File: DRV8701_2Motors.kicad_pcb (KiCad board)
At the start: 4 copper layers, 100 x 40 mm, 92 parts, among them J1 Conn_01x02, J10 Conn_01x04, J11 Conn_01x03, J2 Conn_01x10, J3 Conn_01x10, J4 Conn_01x02, J5 Conn_01x02, J6 Conn_01x04, J7 Conn_ST_STDC14, J8 Conn_01x03, J9 Conn_01x04, SW1 SW_SPDT_321, U16 STM32F303RETx, U3 AM26LV32xD, U4 AM26LV32xD

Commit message: maj README img
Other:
- board text added: "Battery Level"
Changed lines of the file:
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@@
 			(effects
 				(font
-					(size 1 1)
-					(thickness 0.15)
+					(size 0.8 0.5)
+					(thickness 0.1)
+					(bold yes)
 				)
 			)
@@
 			(effects
 				(font
-					(size 1 1)
+					(size 0.8 0.5)
 					(thickness 0.1)
+					(bold yes)
 				)
 			)
@@
 			(effects
 				(font
-					(size 1 1)
+					(size 0.8 0.5)
 					(thickness 0.1)
 				)
@@
 			(effects
 				(font
-					(size 1 1)
+					(size 0.8 0.5)
 					(thickness 0.1)
+					(bold yes)
 				)
 			)
@@
 		(tags "Surface mounted pin header SMD 2x05 1.27mm double row")
 		(property "Reference" "J3"
-			(at 4.8 -1.95 0)
+			(at 4.21 -1.87 0)
 			(layer "F.SilkS")
 			(effects
@@
 		(tags "connector JST PH vertical")
 		(property "Reference" "J11"
-			(at 5.79 -3.31 0)
+			(at 5.9 -2.81 0)
 			(layer "F.SilkS")
 			(effects
 				(font
-					(size 1 1)
-					(thickness 0.15)
+					(size 0.8 0.5)
+					(thickness 0.1)
+					(bold yes)
 				)
 			)
@@
 		(tags "LED RGB NeoPixel PLCC-4 5050")
 		(property "Reference" "D2"
-			(at -0.12 1.79 0)
+			(at -4.17 1.84 0)
 			(layer "F.SilkS")
 			(effects
 				(font
-					(size 1 1)
-					(thickness 0.15)
+					(size 0.8 0.5)
+					(thickness 0.1)
+					(bold yes)
 				)
 			)
@@
 			(effects
 				(font
-					(size 1 1)
-					(thickness 0.15)
+					(size 0.8 0.5)
+					(thickness 0.1)
+					(bold yes)
 				)
 			)
@@
 			(effects
 				(font
-					(size 1 1)
-					(thickness 0.15)
+					(size 0.8 0.5)
+					(thickness 0.1)
+					(bold yes)
 				)
 			)
@@
 			(effects
 				(font
-					(size 1 1)
+					(size 0.8 0.5)
 					(thickness 0.1)
 				)
@@
 			(effects
 				(font
-					(size 1 1)
+					(size 0.8 0.5)
 					(thickness 0.1)
 				)
@@
 			(effects
 				(font
-					(size 0.8 0.8)
+					(size 0.8 0.5)
 					(thickness 0.1)
 					(bold yes)
@@
 			(effects
 				(font
-					(size 1 1)
+					(size 0.8 0.5)
 					(thickness 0.1)
 				)
@@
 			(effects
 				(font
-					(size 1 1)
+					(size 0.8 0.5)
 					(thickness 0.1)
 				)
@@
 			(effects
 				(font
-					(size 1 1)
+					(size 0.8 0.5)
 					(thickness 0.1)
 				)
@@
 			(effects
 				(font
-					(size 1 1)
-					(thickness 0.15)
+					(size 0.8 0.5)
+					(thickness 0.1)
+					(bold yes)
 				)
 			)
@@
 			(effects
 				(font
-					(size 1 1)
+					(size 0.8 0.5)
 					(thickness 0.1)
 				)
@@
 			(effects
 				(font
-					(size 1 1)
-					(thickness 0.15)
+					(size 0.8 0.5)
+					(thickness 0.1)
+					(bold yes)
 				)
 			)
@@
 			(effects
 				(font
-					(size 1 1)
-					(thickness 0.15)
+					(size 0.8 0.5)
+					(thickness 0.1)
+					(bold yes)
 				)
 			)
@@
 			(effects
 				(font
-					(size 1 1)
+					(size 0.8 0.5)
 					(thickness 0.1)
 				)
@@
 			(effects
 				(font
-					(size 1 1)
+					(size 0.8 0.5)
 					(thickness 0.1)
+					(bold yes)
 				)
 			)
@@
 			(effects
 				(font
-					(size 1 1)
-					(thickness 0.15)
+					(size 0.8 0.5)
+					(thickness 0.1)
+					(bold yes)
 				)
 			)
@@
 		(tags "SOIC SO 16-pin-NSOP R-16 R-16-S D0016A M2B SO16 SOT109-1 751B SOIC_N narrow")
 		(property "Reference" "U4"
-			(at 3.025 5.885 0)
+			(at 3.085 6.015 0)
 			(layer "F.SilkS")
 			(effects
@@
 			(effects
 				(font
-					(size 1 1)
-					(thickness 0.15)
+					(size 0.8 0.5)
+					(thickness 0.1)
+					(bold yes)
 				)
 			)
@@
 		(at 169.6 87.69)
 		(property "Reference" "U15"
-			(at -4.2 0.03 0)
+			(at -4.25 -0.04 0)
 			(unlocked yes)
 			(layer "F.SilkS")
@@
 					(size 0.8 0.5)
 					(thickness 0.1)
+					(bold yes)
 				)
 			)
@@
 		(at 132.19 55.21 180)
 		(property "Reference" "J1"
-			(at 2.94 -2.04 0)
+			(at -3.26 -3.34 0)
 			(unlocked yes)
 			(layer "F.SilkS")
 			(effects
 				(font
-					(size 1 1)
+					(size 0.8 0.5)
 					(thickness 0.1)
 				)
@@
 			(effects
 				(font
-					(size 1 1)
+					(size 0.8 0.5)
 					(thickness 0.1)
+					(bold yes)
 				)
 			)
@@
 			(effects
 				(font
-					(size 1 1)
+					(size 0.8 0.5)
 					(thickness 0.1)
 				)
@@
 			(effects
 				(font
-					(size 1 1)
-					(thickness 0.15)
+					(size 0.8 0.5)
+					(thickness 0.1)
+					(bold yes)
 				)
 			)
@@
 			(effects
 				(font
-					(size 1 1)
-					(thickness 0.15)
+					(size 0.8 0.5)
+					(thickness 0.1)
+					(bold yes)
 				)
 			)
@@
 			(effects
 				(font
-					(size 1 1)
-					(thickness 0.15)
+					(size 0.8 0.5)
+					(thickness 0.1)
+					(bold yes)
 				)
 			)
@@
 		(descr "<b>BD45232G-TR-SSOP5</b><br>")
 		(property "Reference" "PS1"
-			(at -3.76 -0.41 180)
+			(at -3.16 -0.06 180)
 			(layer "F.SilkS")
 			(effects
 				(font
-					(size 1 1)
-					(thickness 0.15)
+					(size 0.8 0.5)
+					(thickness 0.1)
+					(bold yes)
 				)
 			)
@@
 			(effects
 				(font
-					(size 1 1)
-					(thickness 0.15)
+					(size 0.8 0.5)
+					(thickness 0.1)
+					(bold yes)
 				)
 			)
@@
 			(effects
 				(font
-					(size 1 1)
+					(size 0.8 0.5)
 					(thickness 0.1)
 				)
@@
 			(effects
 				(font
-					(size 1 1)
-					(thickness 0.15)
+					(size 0.8 0.5)
+					(thickness 0.1)
+					(bold yes)
 				)
 			)
@@
 			(effects
 				(font
-					(size 1 1)
+					(size 0.8 0.5)
 					(thickness 0.1)
 				)
@@
 			(effects
 				(font
-					(size 1 1)
-					(thickness 0.15)
+					(size 0.8 0.5)
+					(thickness 0.1)
+					(bold yes)
 				)
 			)
@@
 			(effects
 				(font
-					(size 1 1)
+					(size 0.8 0.5)
 					(thickness 0.1)
 				)
@@
 			(effects
 				(font
-					(size 1 1)
-					(thickness 0.15)
+					(size 0.8 0.5)
+					(thickness 0.1)
+					(bold yes)
 				)
 			)
@@
 			(effects
 				(font
-					(size 1 1)
-					(thickness 0.15)
+					(size 0.8 0.5)
+					(thickness 0.1)
+					(bold yes)
 				)
 			)
@@
 			(effects
 				(font
-					(size 1 1)
-					(thickness 0.15)
+					(size 0.8 0.5)
+					(thickness 0.1)
+					(bold yes)
 				)
 			)
@@
 		(layer "F.SilkS")
 		(effects
+			(font
+				(size 0.8 0.5)
+				(thickness 0.1)
+				(bold yes)
+			)
+			(justify left bottom)
+		)
+	)
+	(gr_text "Battery Level"
+		(at 129.05 73.95 270)
+		(layer "F.SilkS")
+		(effects

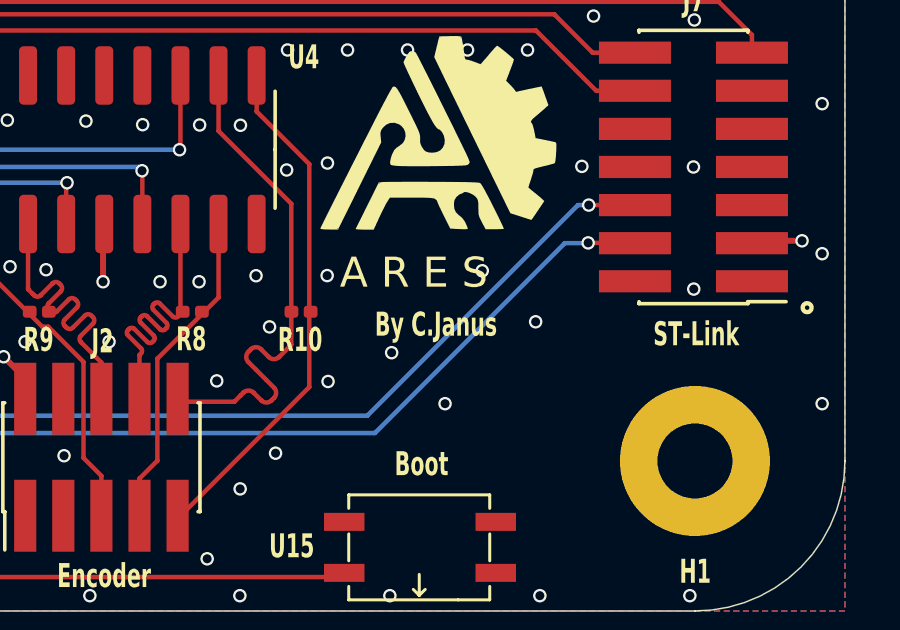
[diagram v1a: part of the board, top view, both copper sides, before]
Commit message: gerber avec reduction 15% du paste
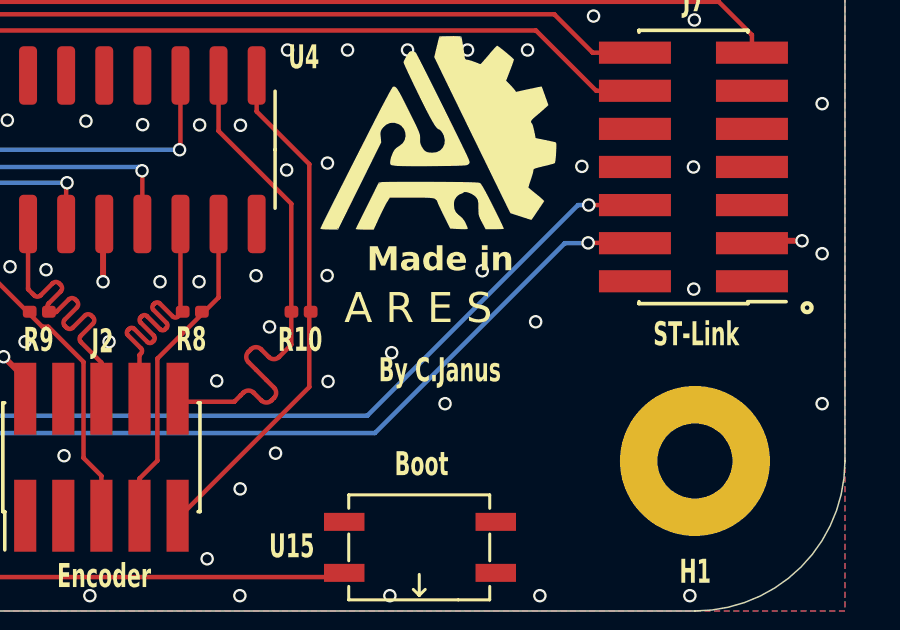
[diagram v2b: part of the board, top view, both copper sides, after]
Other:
- board text added: "Made in"
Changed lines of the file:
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@@
 		)
 		(pad_to_mask_clearance 0)
+		(pad_to_paste_clearance_ratio -0.15)
 		(allow_soldermask_bridges_in_footprints no)
 		(tenting front back)
@@
 	)
 	(gr_text "A R E S "
-		(at 166.95 79.12 0)
+		(at 167.1 80.3 0)
 		(layer "F.SilkS")
 		(effects
@@
 	)
 	(gr_text "By C.Janus"
-		(at 168.12 80.73 0)
+		(at 168.25 82.25 0)
 		(layer "F.SilkS")
 		(effects
@@
 				(thickness 0.1)
 				(bold yes)
+			)
+			(justify left bottom)
+		)
+	)
+	(gr_text "Made in\n"
+		(at 167.85 78.55 0)
+		(layer "F.SilkS")
+		(effects
+			(font
+				(size 0.8 0.8)
+				(thickness 0.1)
+				(bold yes)

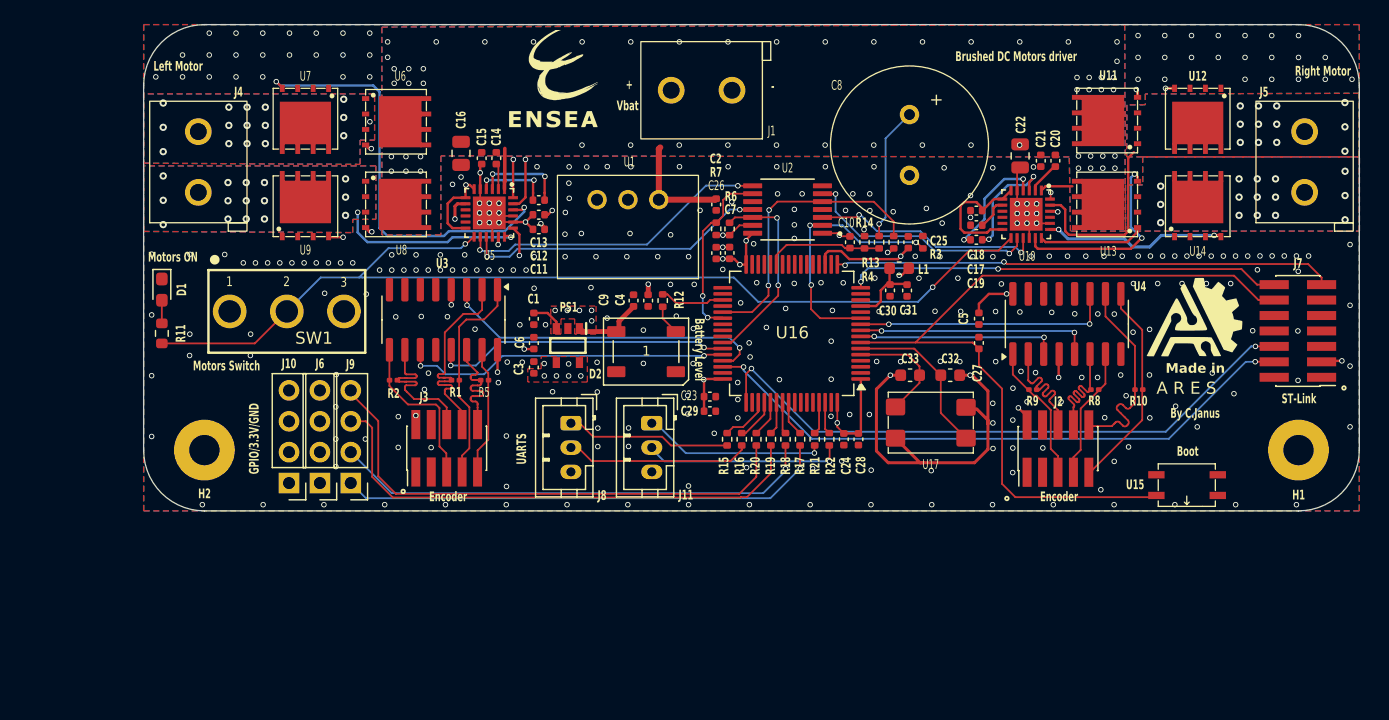
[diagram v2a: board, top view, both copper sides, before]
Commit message: modif footprints des condo de puissance
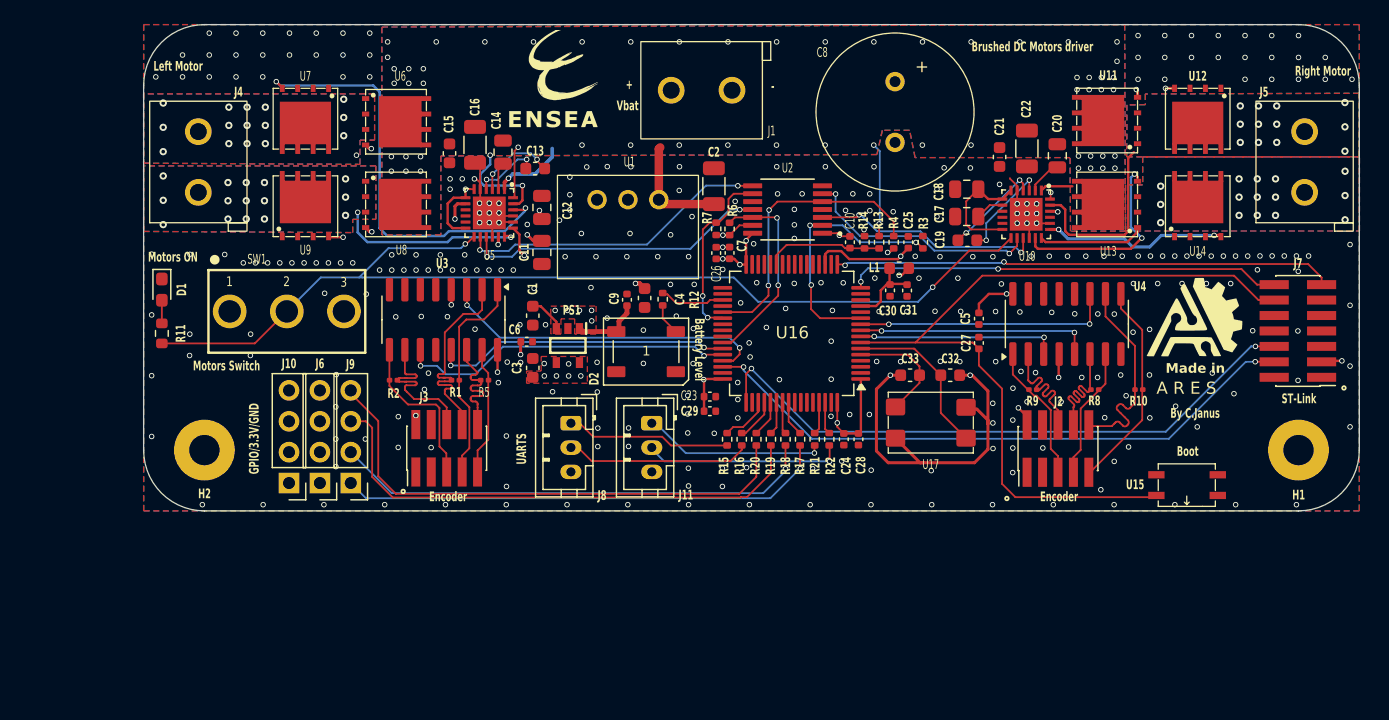
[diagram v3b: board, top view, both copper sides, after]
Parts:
- C1, C13, C15, C19, C21, C3, C4: footprint Capacitor_SMD:C_0402_1005Metric -> Capacitor_SMD:C_0603_1608Metric
- C11, C12, C14, C17, C18, C20: footprint Capacitor_SMD:C_0402_1005Metric -> Capacitor_SMD:C_0805_2012Metric
- C16, C22: footprint Capacitor_SMD:C_0805_2012Metric -> Capacitor_SMD:C_1206_3216Metric
- C2: footprint Capacitor_SMD:C_0402_1005Metric -> Capacitor_SMD:C_1206_3216Metric
- moved C21 3.40 mm to (154.2, 60.7)
- moved C8 2.96 mm to (145.6, 54.5)
- moved C15 2.68 mm to (109.0, 60.4)
- moved C13 2.62 mm to (116.0, 61.6)
- moved C18 1.93 mm to (151.5, 63.4)
- moved C11 1.92 mm to (116.5, 68.5), turned to -90 degrees
- moved C2 1.52 mm to (130.7, 63.1), turned to 90 degrees
- moved C16 1.35 mm to (111.0, 59.7)
- moved C17 1.06 mm to (151.5, 65.6)
- moved C22 0.83 mm to (156.4, 60.0)
- moved C14 0.74 mm to (113.3, 60.3)
- moved C19 0.74 mm to (151.6, 67.5)
- moved C12 0.65 mm to (116.5, 64.8), turned to 90 degrees
- moved C6 0.60 mm to (115.3, 75.9), turned to 0 degrees
- moved C9 0.54 mm to (123.5, 72.5)
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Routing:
- net GND: track 60.1 -> 57.8 mm, vias 327 -> 326
- net Net-(U10-CPH): track 9.42 -> 8.05 mm
- net Net-(U10-CPL): track 9.41 -> 8.10 mm
- net /MoteurDroit/GH2: track 15.8 -> 17.0 mm
- net Net-(U5-AVDD): track 15.6 -> 14.3 mm
- net Net-(U10-AVDD): track 11.0 -> 9.79 mm
- net Net-(U5-CPH): track 7.60 -> 6.83 mm
- net Net-(U5-CPL): track 6.34 -> 5.59 mm
- net VDC: track 26.2 -> 25.5 mm
- net /MoteurDroit/SH2: track 19.1 -> 19.8 mm, vias 17 -> 18
- net /R_ENCA: track 27.1 -> 27.8 mm
- net /MoteurDroit/GL1: track 19.3 -> 19.9 mm
